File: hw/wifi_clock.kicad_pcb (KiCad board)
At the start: 2 copper layers, 80 x 45 mm, 20 parts, among them J1 PicoW right side, J2 DHT22 sensor, U1 74HC595, U2 74HC595, U3 JSD-5613BUA, U4 JSD-5613BUA, U5 JSD-5613BUA, U6 JSD-5613BUA, U7 JSD-5613BUA, U8 JSD-5613BUA

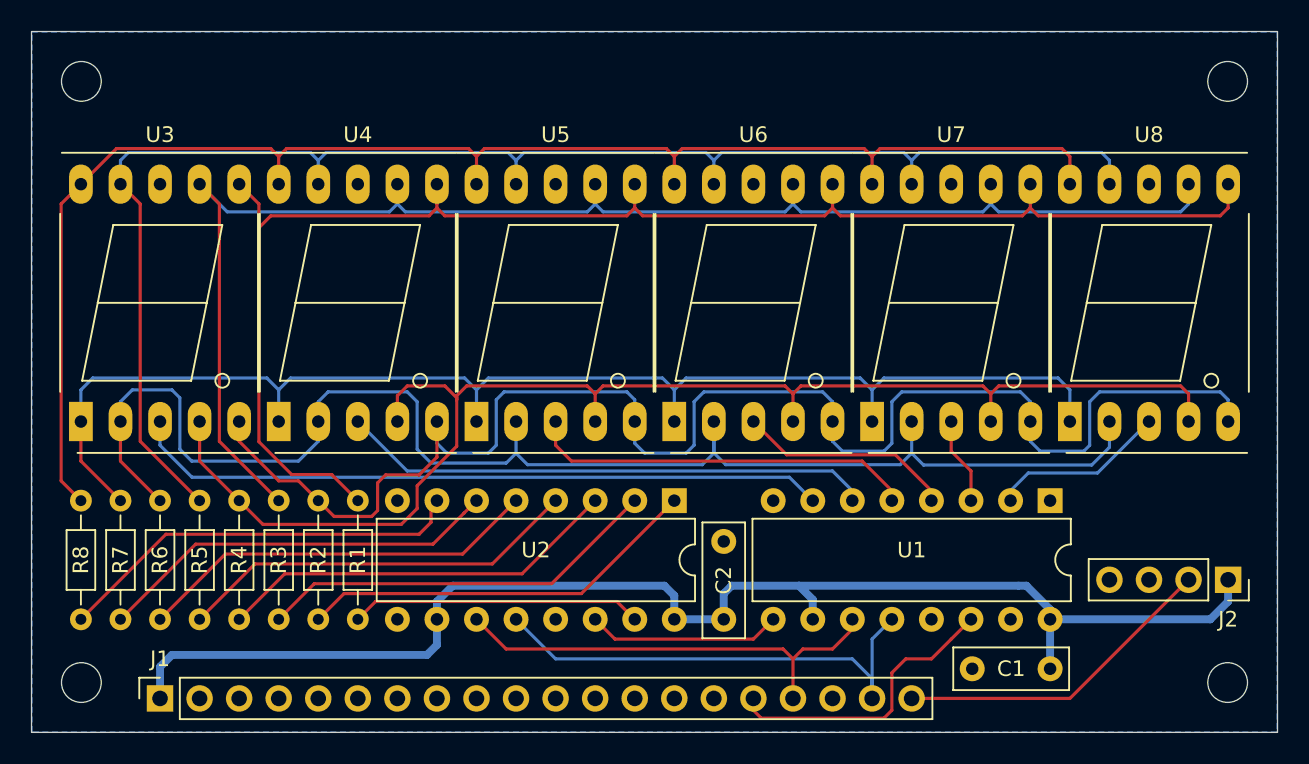
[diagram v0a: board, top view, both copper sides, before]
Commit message: First prototype PCB sent to AISLER manufacturing on 2022-12-15
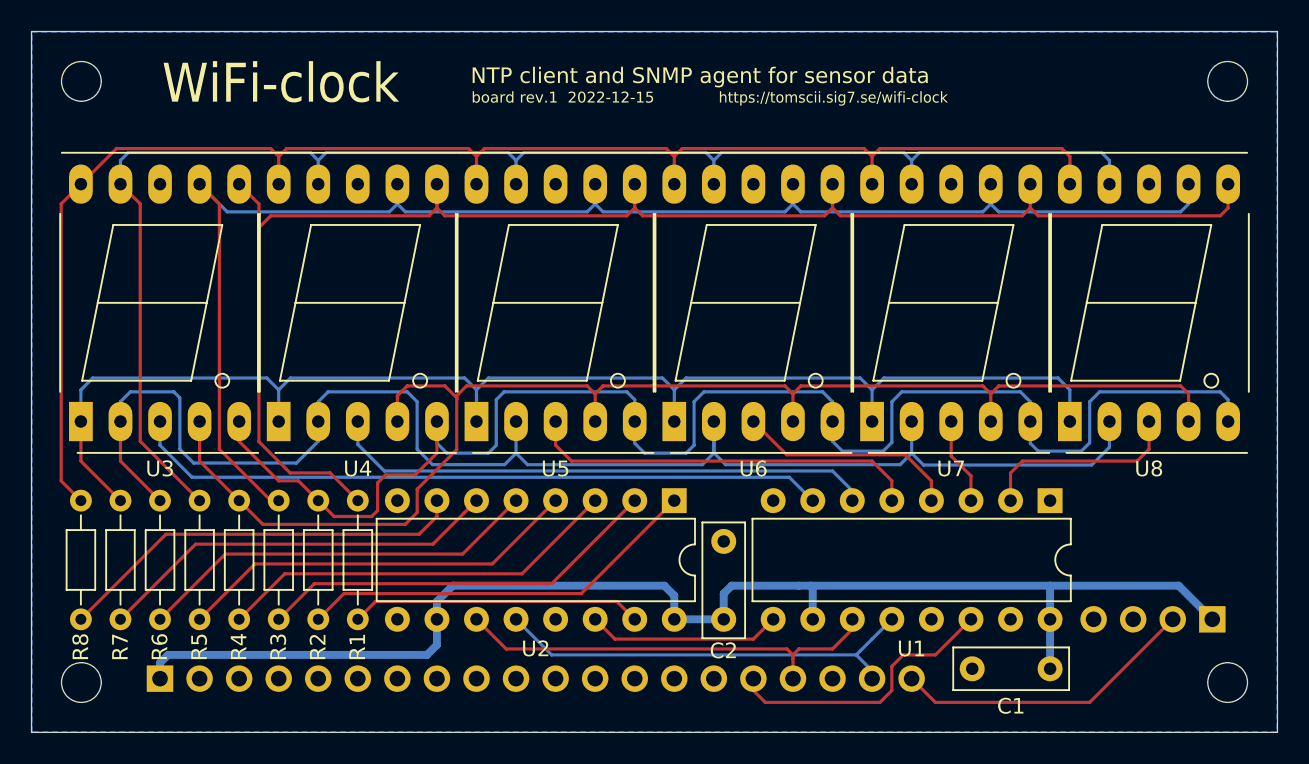
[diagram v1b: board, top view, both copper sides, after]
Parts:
- J1, J2: moved to B.Cu
- moved J2 2.74 mm to (171.7, 111.8), turned to 90 degrees
- moved J1 1.27 mm to (104.1, 115.6), turned to 270 degrees
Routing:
- net /CS-: track 31.3 -> 28.0 mm
- net /VDD: track 86.9 -> 84.4 mm
- net /D5_EN: track 11.4 -> 13.1 mm
- net /DHT22: track 20.9 -> 19.6 mm
- net /SCK: track 29.1 -> 27.9 mm
- net /D1_EN: track 34.2 -> 35.1 mm
- net /SDA: track 19.0 -> 18.2 mm
- net Net-(R8-Pad2): track 26.6 -> 27.2 mm
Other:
- board text added: "DHT"
- board text added: "GND"
- board text added: "NTP client and SNMP agent for sensor data"
- board text added: "SCK"
- board text added: "SDA"
- board text added: "VDD"
- board text added: "WiFi-clock"
- board text added: "board rev.1 2022-12-15"
- board text added: "https://tomscii.sig7.se/wifi-clock"
- board text added: "~CS"
